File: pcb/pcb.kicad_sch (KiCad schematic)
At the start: 4 parts

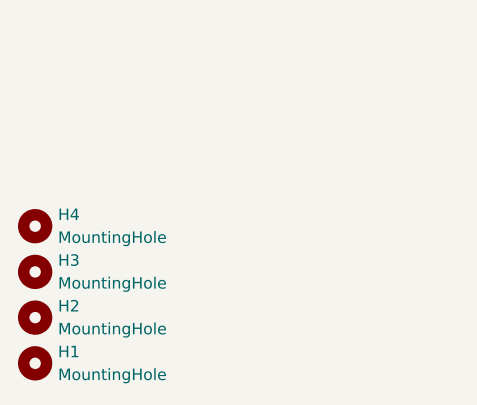
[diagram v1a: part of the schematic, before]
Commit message: feat: switched to cheaper level shifter, re-annotated schematic
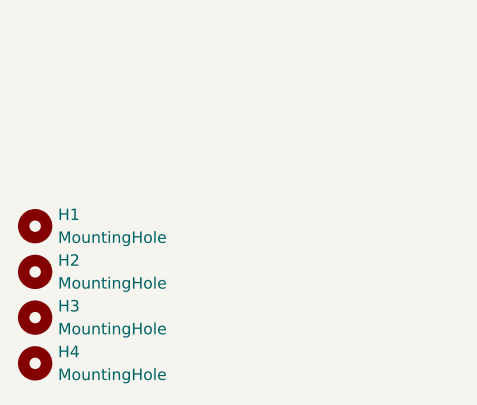
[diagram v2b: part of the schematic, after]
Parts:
- renumbered H4 to H1, H3 to H2, H2 to H3, H1 to H4
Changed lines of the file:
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@@
 		(dnp no)
 		(fields_autoplaced yes)
-		(property "Reference" "H4"
+		(property "Reference" "H1"
 			(at 19.05 176.5299 0)
 			(effects
@@
 			(project ""
 				(path "/9bba97c2-2e09-46fb-bf2a-7de104403c7c"
-					(reference "H4")
+					(reference "H1")
 					(unit 1)
 				)
@@
 		(dnp no)
 		(fields_autoplaced yes)
-		(property "Reference" "H3"
+		(property "Reference" "H2"
 			(at 19.05 181.6099 0)
 			(effects
@@
 			(project ""
 				(path "/9bba97c2-2e09-46fb-bf2a-7de104403c7c"
-					(reference "H3")
+					(reference "H2")
 					(unit 1)
 				)
@@
 		(dnp no)
 		(fields_autoplaced yes)
-		(property "Reference" "H1"
+		(property "Reference" "H4"
 			(at 19.05 191.7699 0)
 			(effects
@@
 			(project ""
 				(path "/9bba97c2-2e09-46fb-bf2a-7de104403c7c"
-					(reference "H1")
+					(reference "H4")
 					(unit 1)
 				)
@@
 		(dnp no)
 		(fields_autoplaced yes)
-		(property "Reference" "H2"
+		(property "Reference" "H3"
 			(at 19.05 186.6899 0)
 			(effects
@@
 			(project ""
 				(path "/9bba97c2-2e09-46fb-bf2a-7de104403c7c"
-					(reference "H2")
+					(reference "H3")
 					(unit 1)
 				)

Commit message: chore: page documentation
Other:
- title: Banshee Microcontroller + Supporting Systems -> Banshee Systems Overview
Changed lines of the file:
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@@
 	(paper "A4")
 	(title_block
-		(title "Banshee Microcontroller + Supporting Systems")
-		(date "2026-02-05")
+		(title "Banshee Systems Overview")
+		(date "2026-02-18")
 		(rev "1")
 		(company "Ivan Leonard O Aparte <ivanleonard.aparte@cit.edu>")
+		(comment 1 "STEM 12 - Altruism | S.Y. 2025-2026")
+		(comment 3 "for Urban Weather Monitoring and AQI Gaps")
+		(comment 4 "OpenPanahon: Experimental Evaluation of a Portable LoRaWAN Mesh")
 	)
 	(wire

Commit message: feat: wiring
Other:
- sheet [1] Power Delivery ports: added I^{2}C_{SCL}, I^{2}C_{SDA}, LOW BATTERY, MCU ~{RESET}; removed none
- sheet [2] System ports: added LOW BATTERY, MCU ~{RESET}, RS485 ~{R}/W, SPI_{1} MISO, SPI_{1} MOSI, SPI_{1} SCK, SPI_{1} ~{CSn}, UART_{0} RX, UART_{0} TX, UART_{1} RX, UART_{1} TX; removed UART ~{R}/W
- sheet [3] Sensors ports: added PM2.5 ~{RESET}, PM2.5 ~{SET}, RS485 ~{READ}/WRITE, UART_{0} RX, UART_{0} TX, UART_{1} RX, UART_{1} TX; removed UART ~{READ}/WRITE

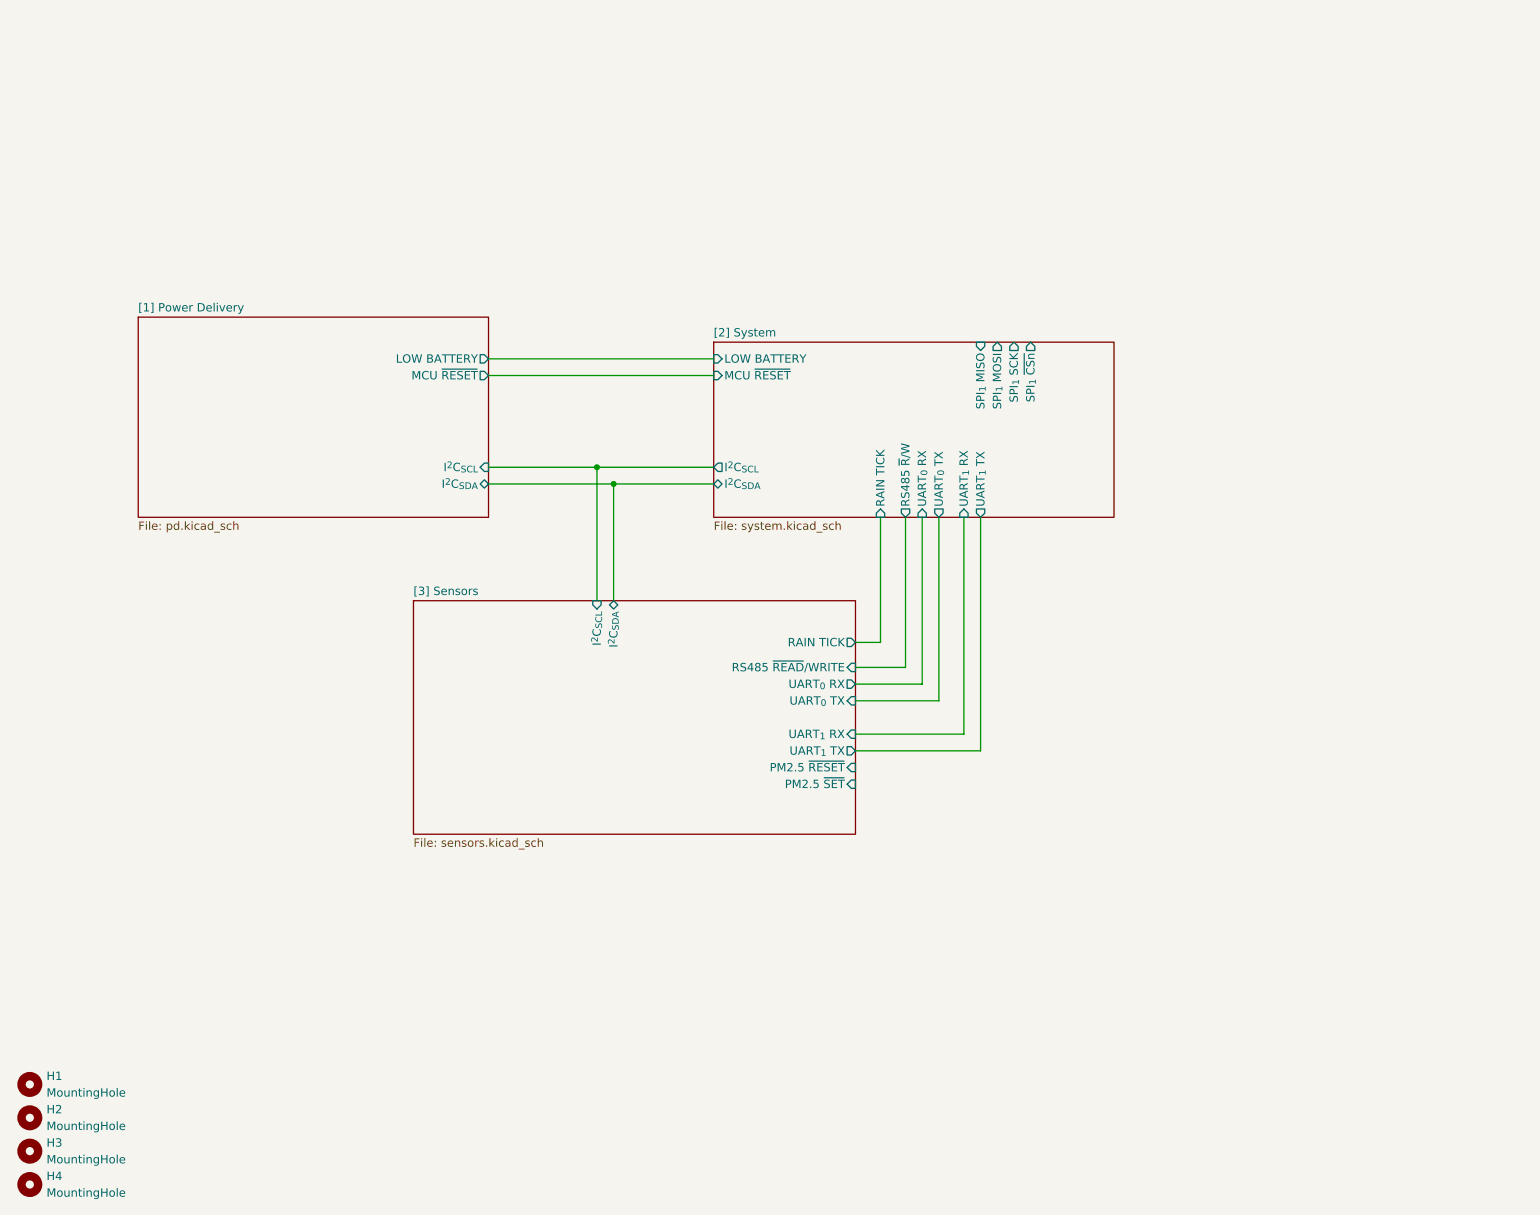
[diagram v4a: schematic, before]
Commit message: feat: radio schematic
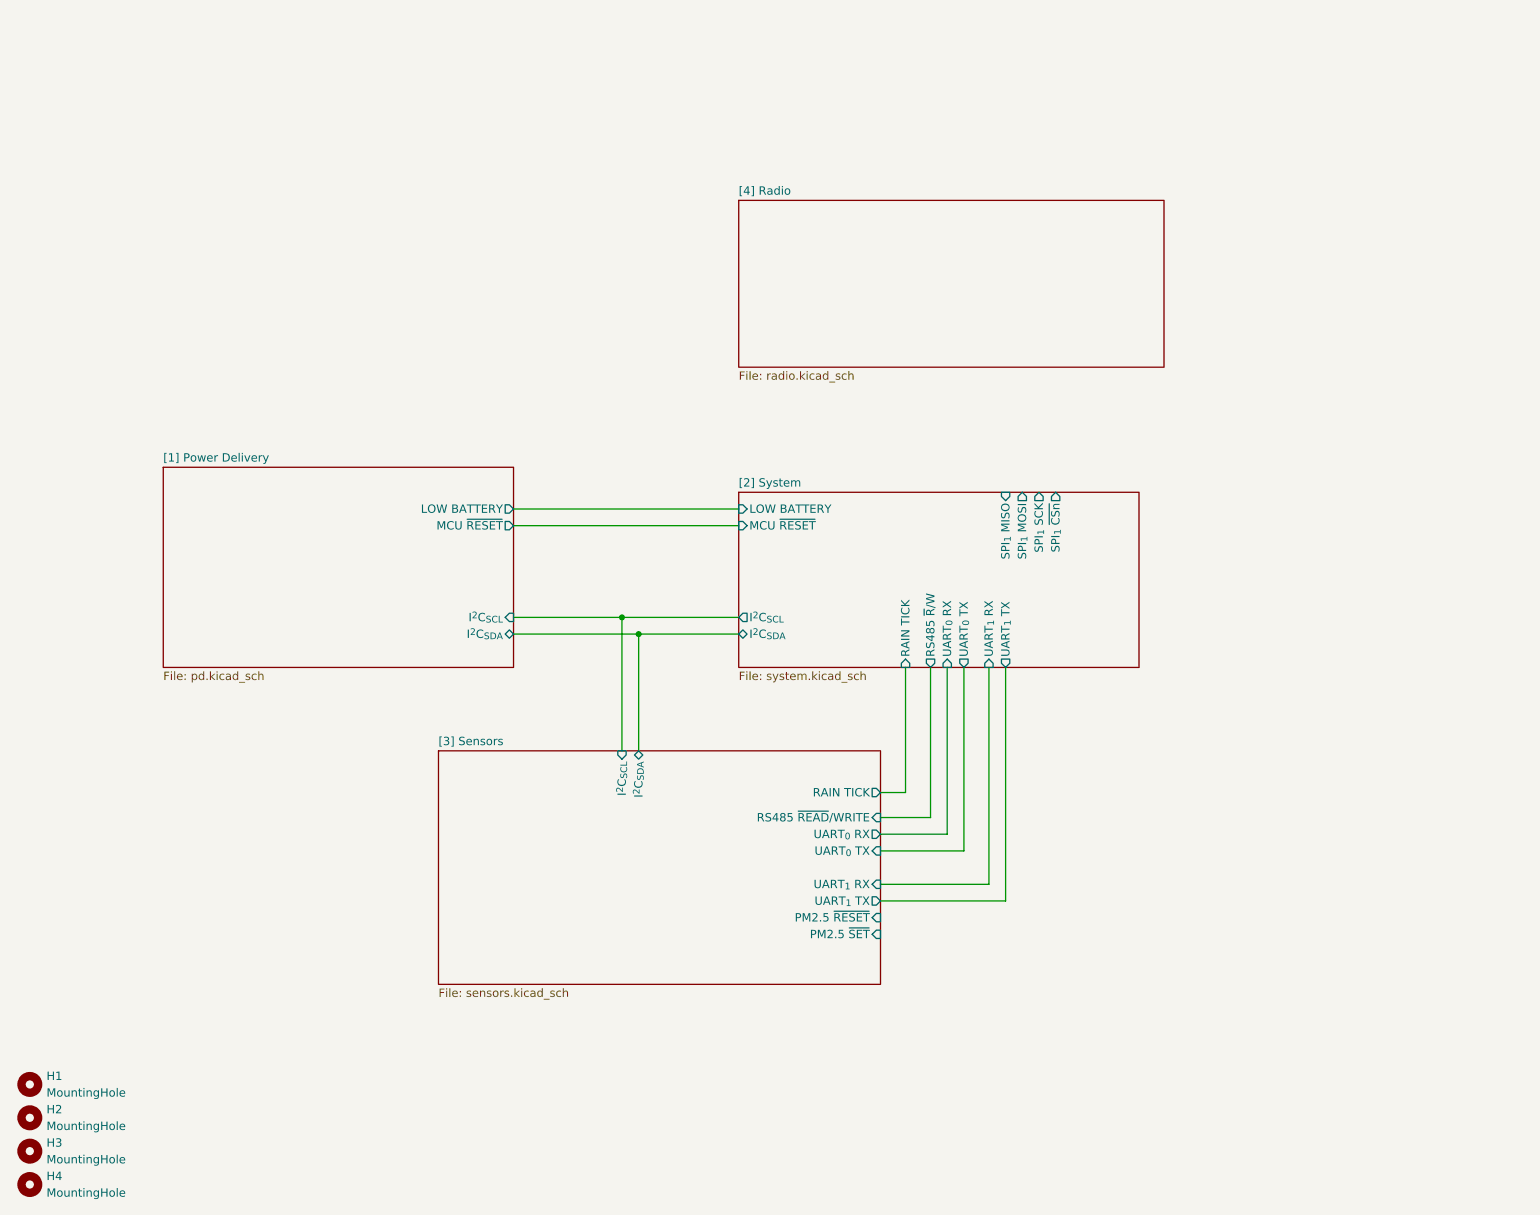
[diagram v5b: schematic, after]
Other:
- added sheet [4] Radio (radio.kicad_sch)
- title: Banshee Systems Overview -> Banshee Power Delivery System

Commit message: feat: revised 3.3v power rail, added power switch
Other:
- sheet [4] Radio ports: added SPI_{1} MISO, SPI_{1} MOSI, SPI_{1} SCK, SPI_{1} ~{CSn}; removed none
- note added: "Passive component values are written according to the metric system. e.g. 10m ohms => 10 milliohms 10M ohms => 10 megaohms"
- note added: "This schematic has been solo'd by one student and his hopes, dreams, and aspirations, coupled with the power of (imaginary) friendship!"
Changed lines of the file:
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@@
 		(comment 4 "OpenPanahon: Experimental Evaluation of a Portable LoRaWAN Mesh")
+	)
+	(text "This schematic has been solo'd by one student\nand his hopes, dreams, and aspirations, coupled\nwith the power of (imaginary) friendship!"
+		(exclude_from_sim no)
+		(at 14.732 29.464 0)
+		(effects
+			(font
+				(size 1.27 1.27)
+				(italic yes)
+			)
+			(justify left)
+		)
+	)
+	(text "Passive component values are written according to\nthe metric system.\n\ne.g. 10m ohms => 10 milliohms\n     10M ohms => 10 megaohms"
+		(exclude_from_sim no)
+		(at 14.732 20.32 0)
+		(effects
+			(font
+				(size 1.27 1.27)
+			)
+			(justify left)
+		)
 	)
 	(junction
@@
 	(wire
 		(pts
+			(xy 170.18 68.58) (xy 170.18 87.63)
+		)
+		(stroke
+			(width 0)
+			(type default)
+		)
+	)
+	(wire
+		(pts
 			(xy 162.56 114.3) (xy 162.56 147.32)
 		)
@@
 	(wire
 		(pts
+			(xy 167.64 68.58) (xy 167.64 87.63)
+		)
+		(stroke
+			(width 0)
+			(type default)
+		)
+	)
+	(wire
+		(pts
 			(xy 158.75 142.24) (xy 146.05 142.24)
 		)
@@
 		(pts
 			(xy 158.75 114.3) (xy 158.75 142.24)
+		)
+		(stroke
+			(width 0)
+			(type default)
+		)
+	)
+	(wire
+		(pts
+			(xy 172.72 68.58) (xy 172.72 87.63)
+		)
+		(stroke
+			(width 0)
+			(type default)
+		)
+	)
+	(wire
+		(pts
+			(xy 165.1 68.58) (xy 165.1 87.63)
 		)
 		(stroke
@@
 			)
 		)
+		(pin "SPI_{1} MISO" output
+			(at 165.1 68.58 270)
+			(effects
+				(font
+					(size 1.27 1.27)
+				)
+				(justify left)
+			)
+		)
+		(pin "SPI_{1} MOSI" input
+			(at 167.64 68.58 270)
+			(effects
+				(font
+					(size 1.27 1.27)
+				)
+				(justify left)
+			)
+		)
+		(pin "SPI_{1} SCK" input
+			(at 170.18 68.58 270)
+			(effects
+				(font
+					(size 1.27 1.27)
+				)
+				(justify left)
+			)
+		)
+		(pin "SPI_{1} ~{CSn}" input
+			(at 172.72 68.58 270)
+			(effects
+				(font
+					(size 1.27 1.27)
+				)
+				(justify left)
+			)
+		)
